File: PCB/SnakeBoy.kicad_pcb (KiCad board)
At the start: 2 copper layers, 180 x 85 mm, 22 parts, among them SW1 X, SW2 A, SW3 Y, SW4 B, SW5 Start, SW6 Select, SW7 Power_SW, U1 ESP32-S3-DEVKITC-1-N16R8, U2 Joystick, U4 TP4056 Module

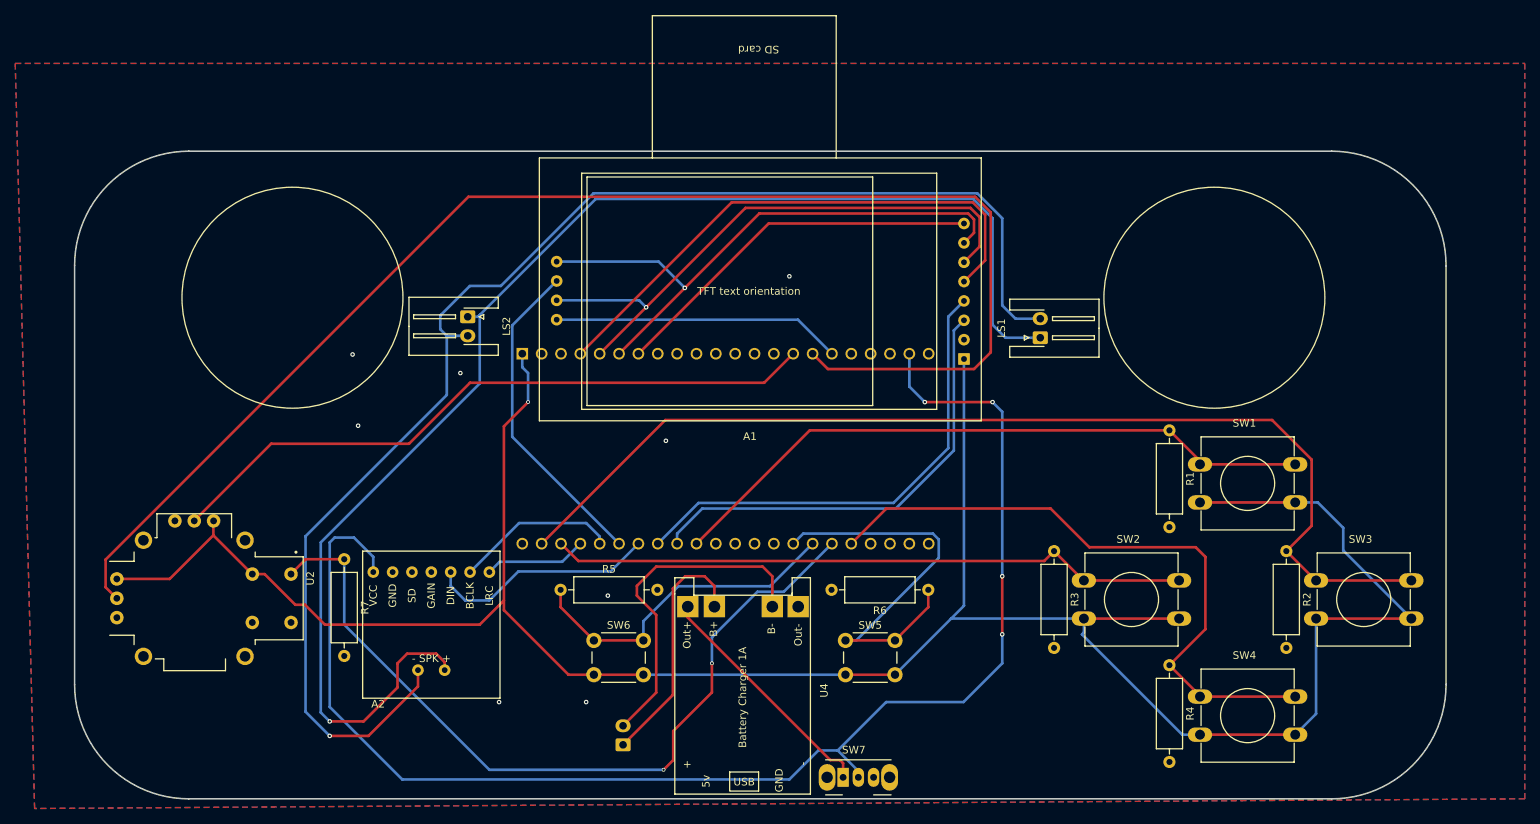
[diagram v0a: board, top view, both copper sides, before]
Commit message: Edited and Retraced the new screen
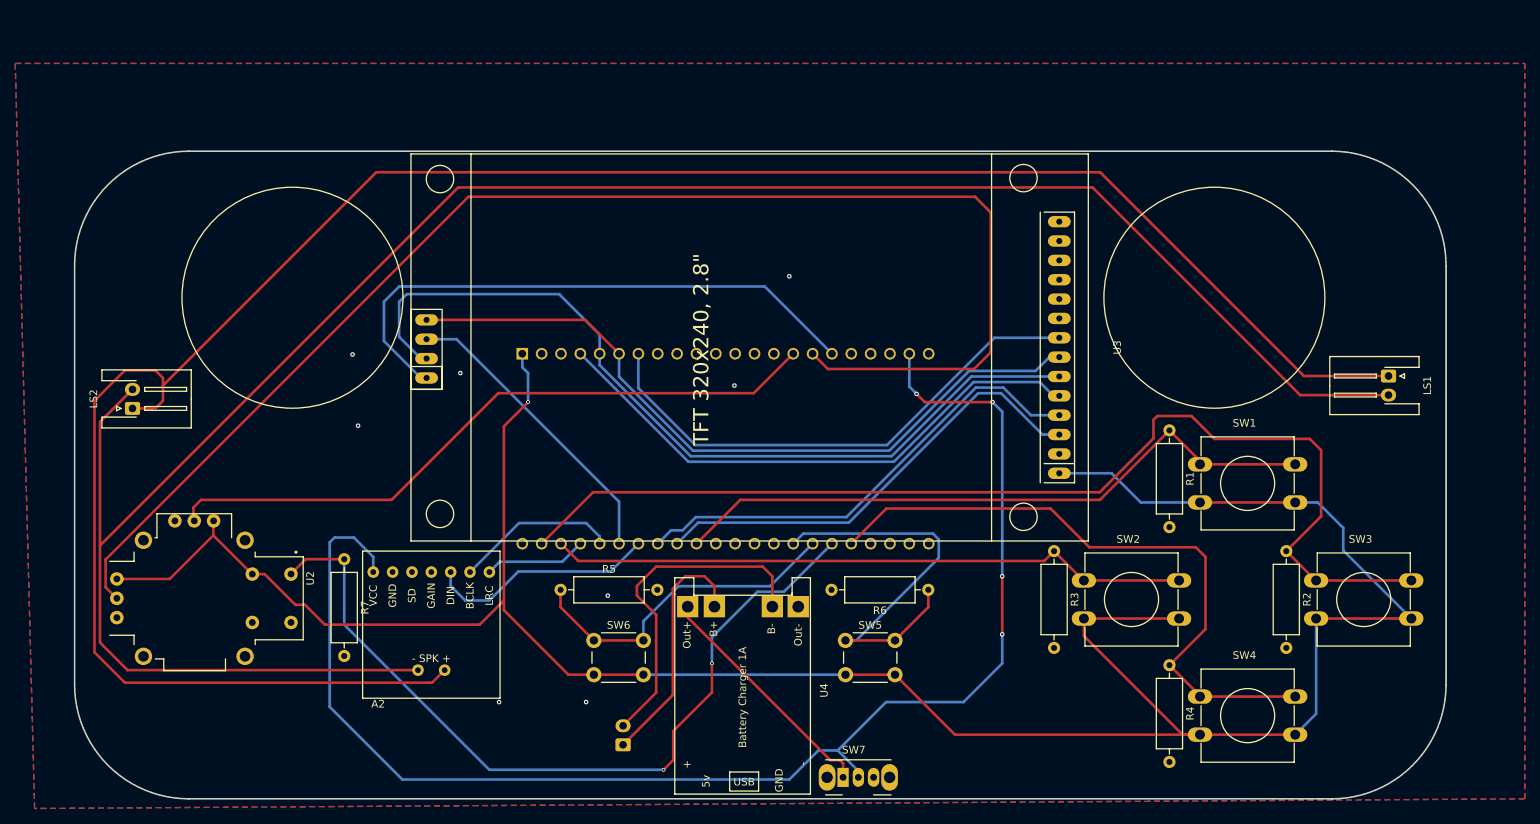
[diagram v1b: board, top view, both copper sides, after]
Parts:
- removed A1: TFT 1.8 inch, Display-extra:Module_TFT_1.8_160x128
- added U3: TFT_320x240, Display-extra:TFT-320x240, F.Cu at (191.6, 83.0)
- moved LS1 46.0 mm to (234.8, 86.8), turned to -90 degrees
- moved LS2 45.6 mm to (70.0, 91.0), turned to 90 degrees
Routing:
- net LOut-: track 181.9 -> 283.3 mm, vias 1 -> 0
- net LOut+: track 182.6 -> 278.1 mm, vias 1 -> 0
- net SD_CS: track 38.0 -> 76.0 mm
- net SD_MOSI: track 77.2 -> 111.9 mm, vias 1 -> 0
- net SD_CLK: track 76.4 -> 97.0 mm, vias 1 -> 0
- net TFT_BL: track 49.8 -> 68.7 mm
- net BT_Y: track 141.3 -> 145.7 mm
- net SD_MISO: track 42.7 -> 39.6 mm
- net TFT_DC: track 72.0 -> 73.8 mm
- net Joy_Y: track 87.7 -> 88.9 mm
- net TFT_RST: track 63.5 -> 62.7 mm
- net TFT_CS: track 59.8 -> 60.6 mm
- net 3v3+: track 326.8 -> 327.3 mm

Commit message: Symetric the Screen
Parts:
- moved U3 3.36 mm to (195.0, 83.0)
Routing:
- net SD_MOSI: track 111.9 -> 118.7 mm
- net TFT_RST: track 62.7 -> 66.0 mm
- net TFT_DC: track 73.8 -> 77.2 mm
- net TFT_BL: track 68.7 -> 72.0 mm
- net 3v3+: track 327.3 -> 323.9 mm
- net TFT_CS: track 60.6 -> 63.9 mm
- net SD_CS: track 76.0 -> 79.4 mm
- net SD_MISO: track 39.6 -> 37.1 mm
